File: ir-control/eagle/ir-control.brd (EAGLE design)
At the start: 47.7 x 35.2 mm, 31 parts, among them J1 MICRO USB, J2 MICRO USB, J3 MICRO USB, Q1 DTA114EET1G (2x10K), Q3 NPN, U2 NUF2042XV6T1G, U3 LPC11U35FHI33/501, U4 MCP1754ST-3302E/CB, X1 KLBR1, Y1 12Mhz

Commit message: Some cleanups.
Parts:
- removed C17: 0.1uF, ir-control:C0402K
- removed D3: LED, ir-control:LED
- removed R13: 1K5, ir-control:R0402
- removed U4: MCP1754ST-3302E/CB, ir-control:SOT-23A
- removed X1: KLBR1, ir-control:KLBR1
- removed Y1: 12Mhz, ir-control:CRYSTAL
- added C9: 0.1uF, ir-control:C0402K
- added D1: LED, ir-control:LED
- added J4: JACKX, ir-control:JACK
- added Q2: 12Mhz, ir-control:CRYSTAL
- added R8: 10K, ir-control:R0402
- added U1: NUF2042XV6T1G, ir-control:SOT-563
- C1: value 18pF -> 10u; device ir-control:C0402K -> ir-control:C0805K
- C2: value 18pF -> 1u; device ir-control:C0402K -> ir-control:C0603K
- C3: value 0.1uF -> 1u; device ir-control:C0402K -> ir-control:C0603K
- C4: value 0.1uF -> 10u; device ir-control:C0402K -> ir-control:C0805K
- C5: value 10u -> 18pF; device ir-control:C0805K -> ir-control:C0402K
- C6: value 1u -> 18pF; device ir-control:C0603K -> ir-control:C0402K
- C7: value 1u -> 0.1uF; device ir-control:C0603K -> ir-control:C0402K
- C8: value 10u -> 0.1uF; device ir-control:C0805K -> ir-control:C0402K
- R1: value 1K5 -> 10K
- R3: value 10K -> 1K5
- R5, R7: value 10K -> 330
- R6: value 330 -> 1K5
- U2: value NUF2042XV6T1G -> MCP1754ST-3302E/CB; device ir-control:SOT-563 -> ir-control:SOT-23A
- moved C5 48.2 mm to (13.0, 46.5), turned to 270 degrees
- moved J2 43.2 mm to (1.50, 8.00), turned to 270 degrees
- moved R4 43.2 mm to (7.62, 44.8), turned to 90 degrees
- moved C8 36.2 mm to (21.3, 39.2)
- moved J3 32.4 mm to (1.50, 42.0)
- moved C6 29.8 mm to (17.9, 46.6), turned to 90 degrees
- moved R7 22.6 mm to (20.4, 31.9), turned to 90 degrees
- moved U3 22.1 mm to (16.5, 39.6)
- moved C7 21.9 mm to (11.6, 42.9), turned to 270 degrees
- moved C4 19.9 mm to (13.7, 28.8), turned to 270 degrees
- moved R2 19.4 mm to (9.06, 10.4), turned to 90 degrees
- moved R3 19.2 mm to (7.62, 37.6), turned to 270 degrees
- moved C3 18.3 mm to (11.4, 29.2), turned to 270 degrees
- moved R6 18.0 mm to (21.0, 26.3), turned to 90 degrees
- moved C1 17.4 mm to (3.30, 29.0), turned to 270 degrees
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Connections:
- net !ISP_EN: now also C9.2; no longer C17.2
- net !RESET: now also R8.1; no longer R3.1
- net +3V3: now also C7.1, C8.1, C9.1, R8.2; no longer C17.1, C3.1, C4.1, R3.2
- net +5V: now also C1.1, C2.1, J3.1, R4.1, R7.2, U1.5, U2.VIN; no longer C5.1, C6.1, J1.1, R2.1, R6.2, U2.5, U4.VIN
- net AV_SENSE: now also R2.2, U3.21; no longer R5.2
- net GND: now also D1.K, Q2.2, Q2.4, U1.2, U2.GND; no longer D3.K, U2.2, U4.GND, Y1.2, Y1.4
- net IR: now also R6.2; no longer R7.2
- net LED: now also R5.1; no longer R13.1
- net N$1: now also C5.1, Q2.3; no longer C1.1, Y1.3
- net N$12: now also J3.2, U1.4; no longer J1.2, U2.4
- net N$14: now also D1.A, R5.2; no longer D3.A, R13.2
- net N$2: now also J1.1, R1.1; no longer J2.1, R4.1
- net N$3: now also C6.1, Q2.1; no longer C2.1, Y1.1
- net N$4: now also R6.1; no longer R7.1
- net N$5: now also R3.2; no longer R1.2
- net N$6: now also J3.3, R3.1, U1.6; no longer J1.3, R1.1, U2.6
- net N$7: now also J2.1, R2.1; no longer J3.1, R5.1
- net TV_SENSE: now also R1.2, U3.19; no longer R4.2
- net USB_DM: now also U1.3; no longer U2.3
- net USB_DP: now also U1.1; no longer U2.1
- net VBUS: now also R4.2; no longer R2.2
- net VOUT: now also C3.1, C4.1, U2.VOUT; no longer C7.1, C8.1, U4.VOUT
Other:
- board size 47.7 x 35.2 mm -> 40 x 50 mm

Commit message: More progress with the layout.
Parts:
- moved R7 7.66 mm to (23.5, 24.8)
- moved R8 7.66 mm to (26.6, 24.9)
- moved C6 7.04 mm to (13.0, 41.6)
- moved C5 6.86 mm to (17.9, 41.7)
- moved R3 6.08 mm to (8.51, 31.6)
- moved Q3 5.84 mm to (28.3, 21.2)
- moved R6 5.67 mm to (23.4, 21.2)
- moved U1 5.48 mm to (8.79, 35.9)
- moved C7 5.14 mm to (11.9, 37.8)
- moved J3 5.02 mm to (2.00, 37.0)
- moved C8 5.01 mm to (21.0, 34.2)
- moved R5 5.00 mm to (28.6, 7.26)
- moved C9 5.00 mm to (24.3, 38.5)
- moved D1 5.00 mm to (33.0, 7.00)
- moved D2 5.00 mm to (18.5, 8.81)
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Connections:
- removed net VOUT: C3.1, C4.1, U2.VOUT
- net +3V3: now also C3.1, C4.1, U2.VOUT
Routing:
- net GND: track 0.00 -> 200.8 mm, vias 0 -> 7
- net +3V3: track 0.00 -> 40.6 mm, vias 0 -> 2
- net +5V: track 0.00 -> 29.6 mm, vias 0 -> 5
- net N$1: track 0.00 -> 7.94 mm
- net USB_DP: track 0.00 -> 6.73 mm
- net N$3: track 0.00 -> 6.00 mm
- net N$12: track 0.00 -> 5.54 mm
- net USB_DM: track 0.00 -> 4.94 mm
- net N$16: track 0.00 -> 4.15 mm
- net !RESET: track 0.00 -> 4.15 mm
- net N$6: track 0.00 -> 3.89 mm
- net LED: track 0.00 -> 0.03 mm, vias 0 -> 1
- added copper zone on layer 16, net GND
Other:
- board size 40 x 50 mm -> 40 x 45 mm

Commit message: More layout cleanup. Still incomplete.
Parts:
- moved J1 12.0 mm to (2.00, 8.00)
- moved J2 12.0 mm to (2.00, 20.0)
- moved R8 5.93 mm to (23.1, 29.7), turned to 180 degrees
- moved Q3 5.34 mm to (28.2, 26.5)
- moved R1 5.26 mm to (9.16, 21.4), turned to 0 degrees
- moved R6 4.12 mm to (23.2, 25.3), turned to 180 degrees
- moved R2 4.02 mm to (9.42, 9.36), turned to 0 degrees
- moved C9 2.98 mm to (21.5, 39.6), turned to 180 degrees
- moved R5 2.75 mm to (27.5, 9.76), turned to 270 degrees
- moved R7 2.73 mm to (23.2, 27.6), turned to 180 degrees
- moved S2 2.42 mm to (23.0, 6.00)
- moved S1 2.29 mm to (15.0, 6.00)
- moved D2 1.82 mm to (18.9, 10.6)
- moved C1 0.64 mm to (4.57, 26.9)
- moved C2 0.64 mm to (6.60, 26.9)
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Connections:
- net N$2: now also J2.1; no longer J1.1
- net N$7: now also J1.1; no longer J2.1
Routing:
- net VBUS: track 0.00 -> 9.47 mm
- net N$6: track 3.89 -> 9.51 mm, vias 0 -> 2
- net !USB_CONNECT: track 0.00 -> 4.39 mm
- net N$5: track 0.00 -> 2.16 mm
- net LED: track 0.03 -> 1.35 mm
- net GND: track 200.8 -> 199.5 mm
- net N$1: track 7.94 -> 8.68 mm
- removed copper zone on layer 16, net GND
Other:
- outline, holes or cut-outs redrawn
- board text added: "AV SENSE"
- board text added: "IR"
- board text added: "IR CONTROLLER"
- board text added: "ISP"
- board text added: "OSH"
- board text added: "PWR"
- board text added: "REV 1.0"
- board text added: "RST"
- board text added: "TV SENSE"

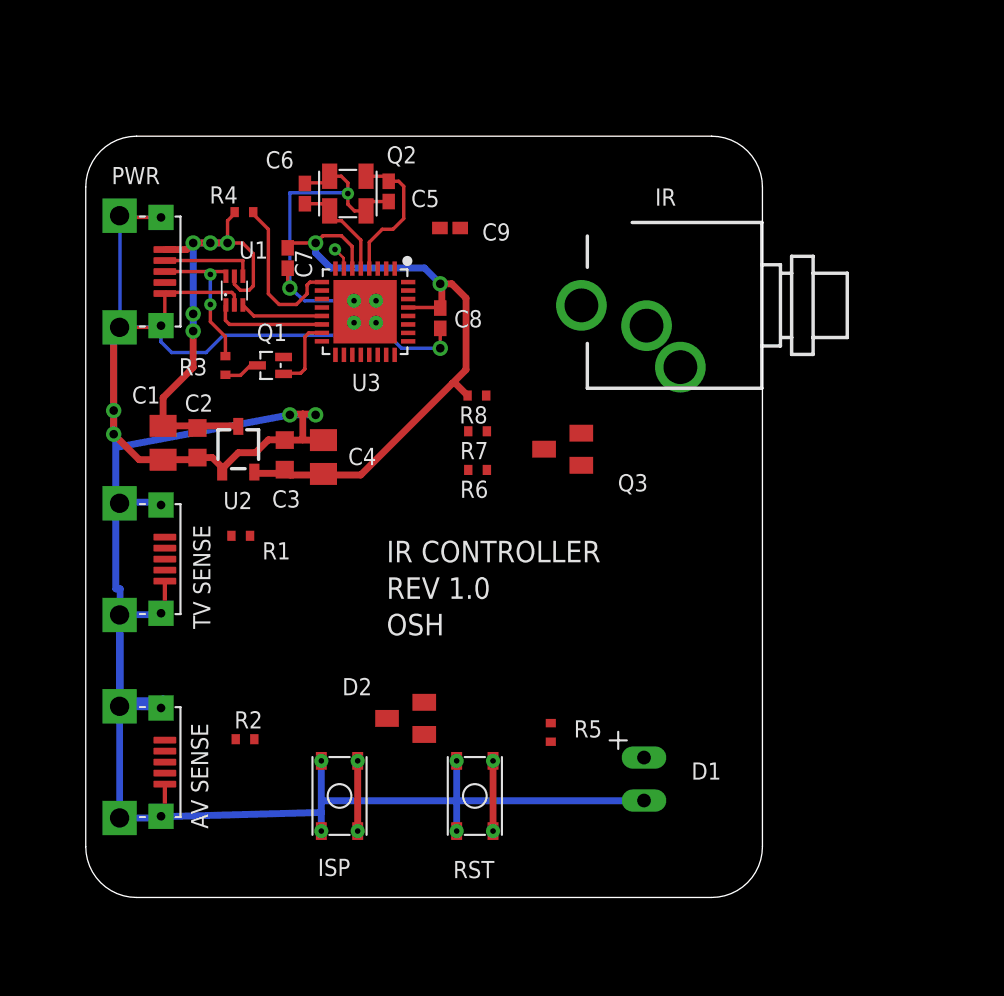
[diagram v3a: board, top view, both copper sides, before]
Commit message: Added ir jack.
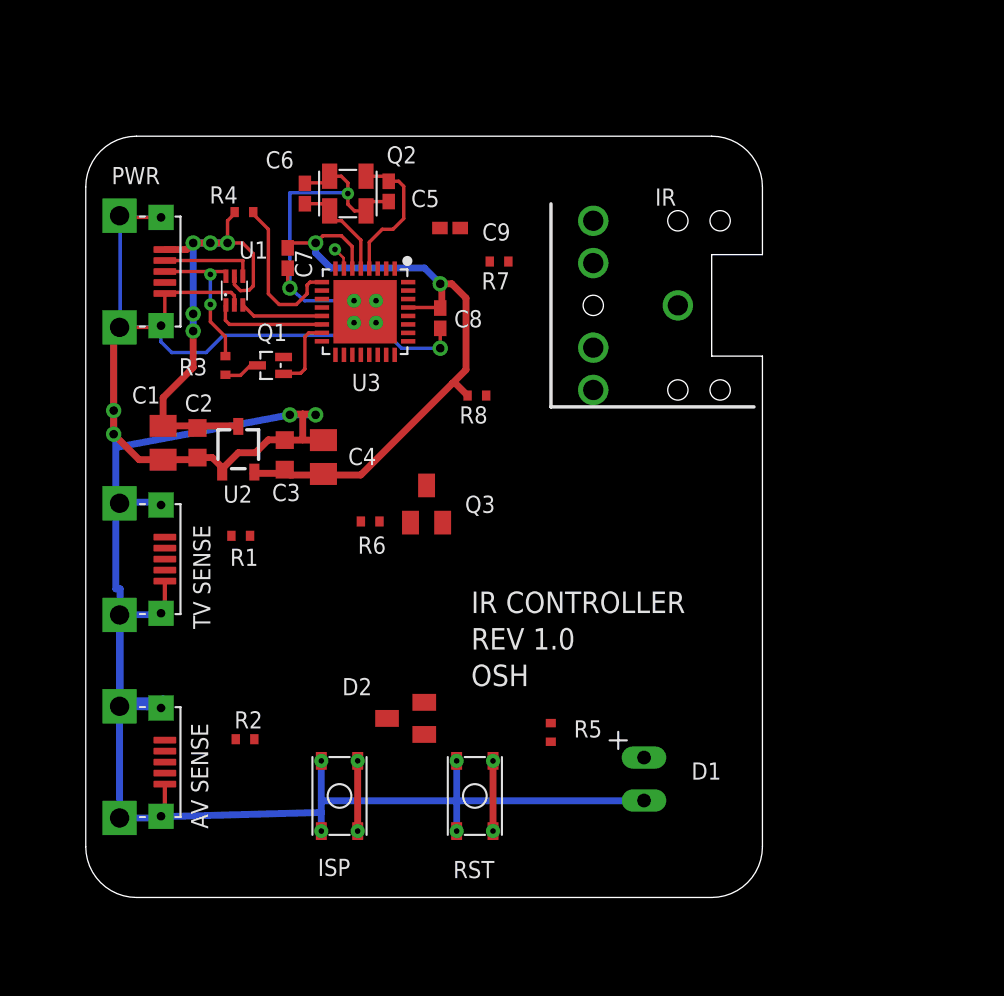
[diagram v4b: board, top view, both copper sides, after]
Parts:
- moved R7 10.1 mm to (24.4, 37.6)
- moved Q3 8.68 mm to (20.1, 23.3), turned to 0 degrees
- moved R6 7.04 mm to (16.8, 22.2)
- moved J4 4.00 mm to (30.0, 35.0), turned to 180 degrees
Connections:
- new net N$8: J4.1, Q3.3
- new net N$9: J4.2, R7.1
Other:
- outline, holes or cut-outs redrawn
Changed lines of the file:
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@@
 <setting verticaltext="up"/>
 </settings>
-<grid distance="5" unitdist="mil" unit="mm" style="lines" multiple="1" display="yes" altdistance="0.025" altunitdist="inch" altunit="inch"/>
+<grid distance="5" unitdist="mil" unit="mm" style="lines" multiple="1" display="yes" altdistance="1" altunitdist="mil" altunit="mil"/>
 <layers>
 <layer number="1" name="Top" color="4" fill="1" visible="yes" active="yes"/>
@@
 <wire x1="3" y1="0" x2="37" y2="0" width="0" layer="20"/>
 <wire x1="37" y1="0" x2="40" y2="3" width="0" layer="20" curve="90"/>
-<wire x1="40" y1="3" x2="40" y2="42" width="0" layer="20"/>
+<wire x1="40" y1="3" x2="40" y2="32" width="0" layer="20"/>
+<wire x1="40" y1="38" x2="40" y2="42" width="0" layer="20"/>
 <wire x1="40" y1="42" x2="37" y2="45" width="0" layer="20" curve="90"/>
 <wire x1="37" y1="45" x2="3" y2="45" width="0" layer="20"/>
@@
 <rectangle x1="-0.381" y1="16.129" x2="0.762" y2="24.003" layer="41"/>
 <rectangle x1="-0.381" y1="4.064" x2="0.762" y2="11.938" layer="41"/>
-<text x="17.78" y="19.812" size="1.27" layer="21" font="vector" ratio="10">IR CONTROLLER</text>
-<text x="17.78" y="17.653" size="1.27" layer="21" font="vector" ratio="10">REV 1.0</text>
-<text x="17.78" y="15.494" size="1.27" layer="21" font="vector" ratio="10">OSH</text>
+<text x="22.78" y="16.812" size="1.27" layer="21" font="vector" ratio="10">IR CONTROLLER</text>
+<text x="22.78" y="14.653" size="1.27" layer="21" font="vector" ratio="10">REV 1.0</text>
+<text x="22.78" y="12.494" size="1.27" layer="21" font="vector" ratio="10">OSH</text>
 <text x="33.655" y="40.894" size="1.016" layer="21" font="vector" ratio="10">IR</text>
+<wire x1="37" y1="32" x2="37" y2="38" width="0" layer="20"/>
+<wire x1="40" y1="38" x2="37" y2="38" width="0" layer="20"/>
+<wire x1="40" y1="32" x2="37" y2="32" width="0" layer="20"/>
 </plain>
 <attributes>
@@
 </element>
 <element name="C3" library="ir-control" package="C0603K" value="1u" x="11.764" y="26.162" smashed="yes" rot="R90">
-<attribute name="NAME" x="11.011" y="23.049" size="1.016" layer="25" font="vector" ratio="10"/>
+<attribute name="NAME" x="11.011" y="23.43" size="1.016" layer="25" font="vector" ratio="10"/>
 </element>
 <element name="D2" library="ir-control" package="SOT23" value="BAS40-05" x="18.909" y="10.585" smashed="yes" rot="R90">
@@
 </element>
 <element name="U2" library="ir-control" package="SOT-23A" value="MCP1754ST-3302E/CB" x="9.017" y="26.496" smashed="yes">
-<attribute name="NAME" x="8.128" y="22.956" size="1.016" layer="25" font="vector" ratio="10"/>
+<attribute name="NAME" x="8.128" y="23.337" size="1.016" layer="25" font="vector" ratio="10"/>
 </element>
 <element name="J2" library="ir-control" package="USB-MICRO" value="MICRO USB" x="2" y="20" smashed="yes" rot="R270"/>
 <element name="J1" library="ir-control" package="USB-MICRO" value="MICRO USB" x="2" y="8" smashed="yes" rot="R270"/>
 <element name="R1" library="ir-control" package="R0402" value="10K" x="9.162" y="21.379" smashed="yes">
-<attribute name="NAME" x="10.432" y="19.982" size="1.016" layer="25" font="vector" ratio="10"/>
+<attribute name="NAME" x="8.527" y="19.601" size="1.016" layer="25" font="vector" ratio="10"/>
 </element>
 <element name="R2" library="ir-control" package="R0402" value="10K" x="9.416" y="9.355" smashed="yes">
 <attribute name="NAME" x="8.781" y="9.99" size="1.016" layer="25" font="vector" ratio="10"/>
 </element>
-<element name="J4" library="ir-control" package="JACK" value="JACKX" x="34" y="35" smashed="yes" rot="R270">
-<attribute name="OC_NEWARK" value="97K2707" x="34" y="35" size="1.778" layer="27" rot="R270" display="off"/>
-<attribute name="OC_FARNELL" value="1200140" x="34" y="35" size="1.778" layer="27" rot="R270" display="off"/>
-<attribute name="MPN" value="KLBR 1" x="34" y="35" size="1.778" layer="27" rot="R270" display="off"/>
-<attribute name="MF" value="" x="34" y="35" size="1.778" layer="27" rot="R270" display="off"/>
-</element>
-<element name="R7" library="ir-control" package="R0402" value="330" x="23.161" y="27.559" smashed="yes" rot="R180">
-<attribute name="NAME" x="23.796" y="26.924" size="1.016" layer="25" font="vector" ratio="10" rot="R180"/>
-</element>
-<element name="Q3" library="ir-control" package="SOT23" value="NPN" x="28.194" y="26.496" smashed="yes" rot="R90">
-<attribute name="NAME" x="31.449" y="24.003" size="1.016" layer="25" font="vector" ratio="10"/>
-</element>
-<element name="R6" library="ir-control" package="R0402" value="1K5" x="23.161" y="25.273" smashed="yes" rot="R180">
-<attribute name="NAME" x="23.796" y="24.638" size="1.016" layer="25" font="vector" ratio="10" rot="R180"/>
+<element name="J4" library="ir-control" package="JACK" value="JACKX" x="30" y="35" smashed="yes" rot="R180">
+<attribute name="OC_NEWARK" value="97K2707" x="30" y="35" size="1.778" layer="27" rot="R180" display="off"/>
+<attribute name="OC_FARNELL" value="1200140" x="30" y="35" size="1.778" layer="27" rot="R180" display="off"/>
+<attribute name="MPN" value="KLBR 1" x="30" y="35" size="1.778" layer="27" rot="R180" display="off"/>
+<attribute name="MF" value="" x="30" y="35" size="1.778" layer="27" rot="R180" display="off"/>
+</element>
+<element name="R7" library="ir-control" package="R0402" value="330" x="24.431" y="37.592" smashed="yes" rot="R180">
+<attribute name="NAME" x="25.066" y="36.957" size="1.016" layer="25" font="vector" ratio="10" rot="R180"/>
+</element>
+<element name="Q3" library="ir-control" package="SOT23" value="NPN" x="20.146" y="23.257" smashed="yes">
+<attribute name="NAME" x="22.416" y="22.733" size="1.016" layer="25" font="vector" ratio="10"/>
+</element>
+<element name="R6" library="ir-control" package="R0402" value="1K5" x="16.811" y="22.225" smashed="yes" rot="R180">
+<attribute name="NAME" x="16.082" y="20.32" size="1.016" layer="25" font="vector" ratio="10"/>
 </element>
 </elements>
@@
 <wire x1="2.032" y1="40.212" x2="4.445" y2="40.212" width="0.2032" layer="16"/>
 <wire x1="4.445" y1="40.212" x2="4.445" y2="40.085" width="0.2032" layer="16"/>
-<wire x1="8.786" y1="35.025" x2="8.786" y2="35.617" width="0.2032" layer="1"/>
-<wire x1="8.786" y1="35.617" x2="8.636" y2="35.767" width="0.2032" layer="1"/>
-<wire x1="8.636" y1="35.767" x2="4.742" y2="35.767" width="0.2032" layer="1"/>
+<wire x1="8.786" y1="35.025" x2="8.786" y2="35.5662" width="0.2032" layer="1"/>
+<wire x1="8.786" y1="35.5662" x2="8.5852" y2="35.767" width="0.2032" layer="1"/>
+<wire x1="8.5852" y1="35.767" x2="4.742" y2="35.767" width="0.2032" layer="1"/>
 <wire x1="4.742" y1="35.767" x2="4.675" y2="35.7" width="0.2032" layer="1"/>
 <wire x1="2" y1="33.7" x2="1.651" y2="33.351" width="0.4064" layer="1"/>
@@
 <wire x1="15.494" y1="42.244" x2="15.494" y2="41.656" width="0" layer="19" extent="1-16"/>
 <wire x1="4.445" y1="23.368" x2="4.572" y2="25.877" width="0" layer="19" extent="1-16"/>
-<wire x1="29.294" y1="27.446" x2="20.955" y2="32.465" width="0" layer="19" extent="1-1"/>
+<wire x1="21.096" y1="22.157" x2="20.955" y2="32.465" width="0" layer="19" extent="1-1"/>
 </signal>
 <signal name="+5V">
@@
 <contactref element="R7" pad="2"/>
 <wire x1="9.652" y1="35.894" x2="9.906" y2="36.148" width="0.2032" layer="1"/>
-<wire x1="8.786" y1="36.725" x2="8.786" y2="36.252" width="0.2032" layer="1"/>
-<wire x1="8.786" y1="36.252" x2="9.144" y2="35.894" width="0.2032" layer="1"/>
-<wire x1="9.144" y1="35.894" x2="9.652" y2="35.894" width="0.2032" layer="1"/>
+<wire x1="8.786" y1="36.725" x2="8.786" y2="36.2266" width="0.2032" layer="1"/>
+<wire x1="8.786" y1="36.2266" x2="9.144" y2="35.8686" width="0.2032" layer="1"/>
+<wire x1="9.144" y1="35.8686" x2="9.652" y2="35.894" width="0.2032" layer="1"/>
 <via x="6.35" y="38.688" extent="1-16" drill="0.508"/>
 <via x="7.366" y="38.688" extent="1-16" drill="0.508"/>
@@
 <wire x1="6.35" y1="31.322" x2="4.572" y2="29.544" width="0.4064" layer="1"/>
 <wire x1="4.572" y1="29.544" x2="4.572" y2="27.877" width="0.4064" layer="1"/>
-<wire x1="9.017" y1="27.846" x2="22.611" y2="27.559" width="0" layer="19" extent="1-1"/>
+<wire x1="9.017" y1="27.846" x2="23.881" y2="37.592" width="0" layer="19" extent="1-1"/>
 </signal>
 <signal name="N$6">
@@
 <contactref element="R6" pad="1"/>
 <contactref element="Q3" pad="1"/>
-<wire x1="23.711" y1="25.273" x2="29.294" y2="25.546" width="0" layer="19" extent="1-1"/>
+<wire x1="17.361" y1="22.225" x2="19.196" y2="22.157" width="0" layer="19" extent="1-1"/>
 </signal>
 <signal name="IR">
 <contactref element="R6" pad="2"/>
 <contactref element="U3" pad="17"/>
-<wire x1="14.76" y1="32.074" x2="22.611" y2="25.273" width="0" layer="19" extent="1-1"/>
+<wire x1="14.76" y1="32.074" x2="16.261" y2="22.225" width="0" layer="19" extent="1-1"/>
+</signal>
+<signal name="N$8">
+<contactref element="J4" pad="1"/>
+<contactref element="Q3" pad="3"/>
+<wire x1="20.146" y1="24.357" x2="35" y2="35" width="0" layer="19" extent="1-1"/>
+</signal>
+<signal name="N$9">
+<contactref element="J4" pad="2"/>
+<contactref element="R7" pad="1"/>
+<wire x1="24.981" y1="37.592" x2="30" y2="40" width="0" layer="19" extent="1-1"/>
 </signal>
 </signals>
